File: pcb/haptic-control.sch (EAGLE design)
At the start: 131 parts, among them M1 SPH0641LM4H-1, P1 2P-PAD_1X3.5, P2 2P-PAD_1X3.5, P3 2P-PAD_1X3.5, P4 2P-PAD_1X3.5, U1 MIC23159, U10 DRV2605L, U11 DRV2605L, U12 MTCH6301, U2 BQ51050B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

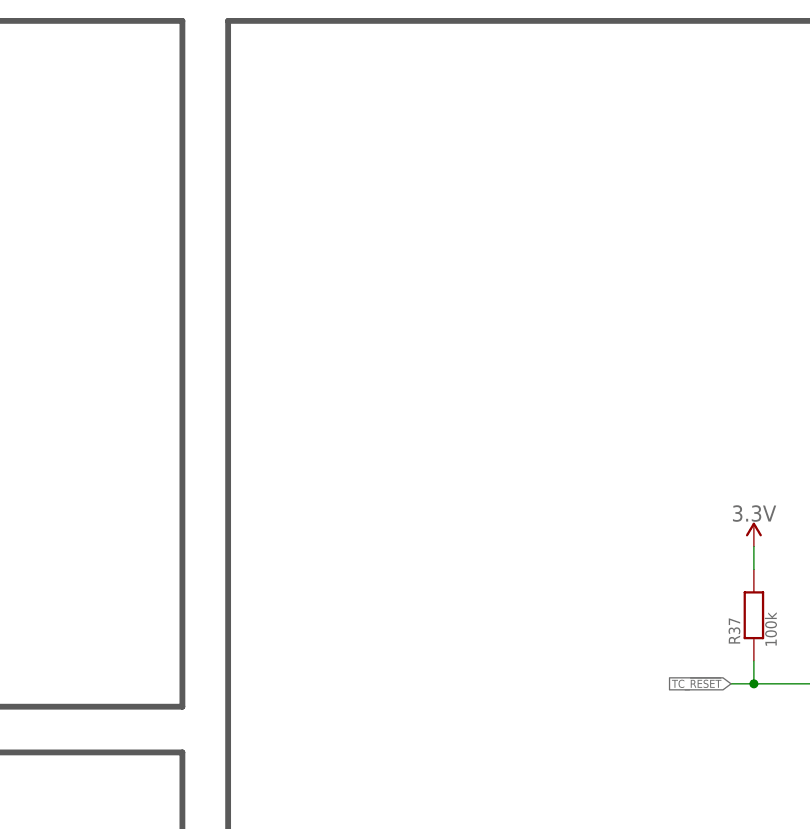
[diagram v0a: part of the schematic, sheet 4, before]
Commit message: Add pcap touch panel
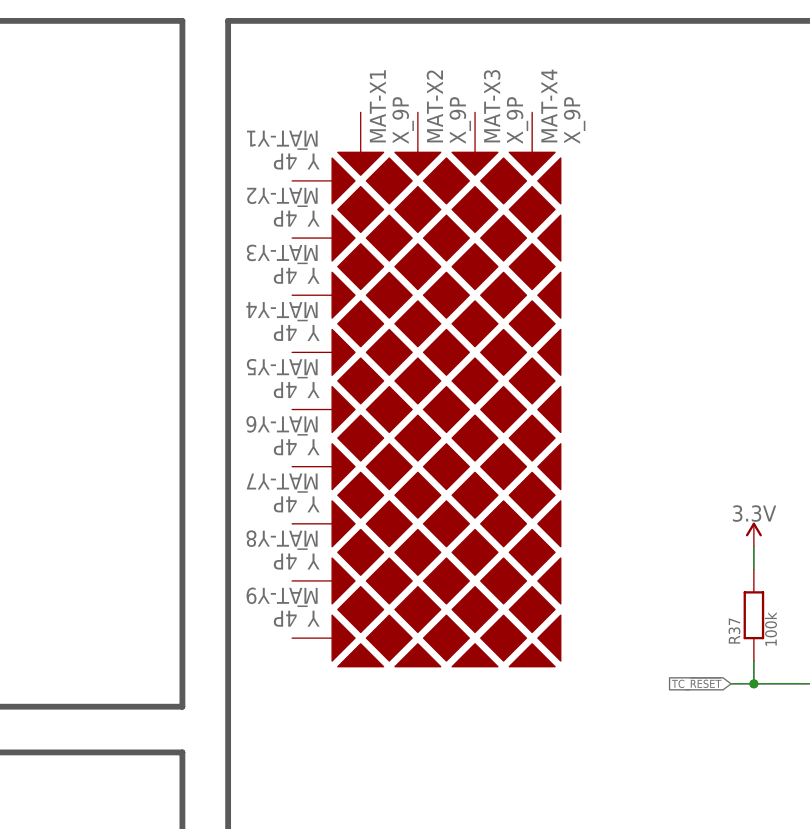
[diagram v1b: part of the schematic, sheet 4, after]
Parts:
- added MAT-X1, MAT-X2, MAT-X3, MAT-X4: X_9P, Touch Panel:X_9P
- added MAT-Y1, MAT-Y2, MAT-Y3, MAT-Y4, MAT-Y5, MAT-Y6, MAT-Y7, MAT-Y8, MAT-Y9: Y_4P, Touch Panel:Y_4P
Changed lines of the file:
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@@
 <part name="C11" library="Passive Components &gt; Capacitors &gt; Multilayer Ceramic Capacitors MLCC" deviceset="MLCC" device="_0402" value="470n"/>
 <part name="JP3" library="Utility &gt; Board" deviceset="JUMPER-SMT_2_NC_TRACE" device="_SILK"/>
+<part name="MAT-X1" library="Touch Panel" deviceset="X_9P" device=""/>
+<part name="MAT-X2" library="Touch Panel" deviceset="X_9P" device=""/>
+<part name="MAT-X3" library="Touch Panel" deviceset="X_9P" device=""/>
+<part name="MAT-X4" library="Touch Panel" deviceset="X_9P" device=""/>
+<part name="MAT-Y1" library="Touch Panel" deviceset="Y_4P" device=""/>
+<part name="MAT-Y2" library="Touch Panel" deviceset="Y_4P" device=""/>
+<part name="MAT-Y3" library="Touch Panel" deviceset="Y_4P" device=""/>
+<part name="MAT-Y4" library="Touch Panel" deviceset="Y_4P" device=""/>
+<part name="MAT-Y5" library="Touch Panel" deviceset="Y_4P" device=""/>
+<part name="MAT-Y6" library="Touch Panel" deviceset="Y_4P" device=""/>
+<part name="MAT-Y7" library="Touch Panel" deviceset="Y_4P" device=""/>
+<part name="MAT-Y8" library="Touch Panel" deviceset="Y_4P" device=""/>
+<part name="MAT-Y9" library="Touch Panel" deviceset="Y_4P" device=""/>
 </parts>
 <sheets>
@@
 <attribute name="VALUE" x="180.34" y="124.206" size="1.778" layer="96" align="top-center"/>
 </instance>
+<instance part="MAT-X1" gate="G$1" x="228.092" y="203.2" smashed="yes">
+<attribute name="VALUE" x="231.648" y="232.664" size="1.778" layer="96" ratio="10" rot="SR90" align="top-left"/>
+<attribute name="NAME" x="229.108" y="232.664" size="1.778" layer="95" ratio="10" rot="SR90" align="top-left"/>
+</instance>
+<instance part="MAT-X2" gate="G$1" x="234.442" y="203.2" smashed="yes">
+<attribute name="VALUE" x="237.998" y="232.664" size="1.778" layer="96" ratio="10" rot="SR90" align="top-left"/>
+<attribute name="NAME" x="235.458" y="232.664" size="1.778" layer="95" ratio="10" rot="SR90" align="top-left"/>
+</instance>
+<instance part="MAT-X3" gate="G$1" x="240.792" y="203.2" smashed="yes">
+<attribute name="VALUE" x="244.348" y="232.664" size="1.778" layer="96" ratio="10" rot="SR90" align="top-left"/>
+<attribute name="NAME" x="241.808" y="232.664" size="1.778" layer="95" ratio="10" rot="SR90" align="top-left"/>
+</instance>
+<instance part="MAT-X4" gate="G$1" x="247.142" y="203.2" smashed="yes">
+<attribute name="VALUE" x="250.698" y="232.664" size="1.778" layer="96" ratio="10" rot="SR90" align="top-left"/>
+<attribute name="NAME" x="248.158" y="232.664" size="1.778" layer="95" ratio="10" rot="SR90" align="top-left"/>
+</instance>
+<instance part="MAT-Y1" gate="G$1" x="237.617" y="228.6" smashed="yes">
+<attribute name="VALUE" x="223.52" y="229.87" size="1.778" layer="96" ratio="10" rot="SR180" align="top-left"/>
+<attribute name="NAME" x="223.52" y="232.41" size="1.778" layer="95" ratio="10" rot="SR180" align="top-left"/>
+</instance>
+<instance part="MAT-Y2" gate="G$1" x="237.617" y="222.25" smashed="yes">
+<attribute name="VALUE" x="223.52" y="223.52" size="1.778" layer="96" ratio="10" rot="SR180" align="top-left"/>
+<attribute name="NAME" x="223.52" y="226.06" size="1.778" layer="95" ratio="10" rot="SR180" align="top-left"/>
+</instance>
+<instance part="MAT-Y3" gate="G$1" x="237.617" y="215.9" smashed="yes">
+<attribute name="VALUE" x="223.52" y="217.17" size="1.778" layer="96" ratio="10" rot="SR180" align="top-left"/>
+<attribute name="NAME" x="223.52" y="219.71" size="1.778" layer="95" ratio="10" rot="SR180" align="top-left"/>
+</instance>
+<instance part="MAT-Y4" gate="G$1" x="237.617" y="209.55" smashed="yes">
+<attribute name="VALUE" x="223.52" y="210.82" size="1.778" layer="96" ratio="10" rot="SR180" align="top-left"/>
+<attribute name="NAME" x="223.52" y="213.36" size="1.778" layer="95" ratio="10" rot="SR180" align="top-left"/>
+</instance>
+<instance part="MAT-Y5" gate="G$1" x="237.617" y="203.2" smashed="yes">
+<attribute name="VALUE" x="223.52" y="204.47" size="1.778" layer="96" ratio="10" rot="SR180" align="top-left"/>
+<attribute name="NAME" x="223.52" y="207.01" size="1.778" layer="95" ratio="10" rot="SR180" align="top-left"/>
+</instance>
+<instance part="MAT-Y6" gate="G$1" x="237.617" y="196.85" smashed="yes">
+<attribute name="VALUE" x="223.52" y="198.12" size="1.778" layer="96" ratio="10" rot="SR180" align="top-left"/>
+<attribute name="NAME" x="223.52" y="200.66" size="1.778" layer="95" ratio="10" rot="SR180" align="top-left"/>
+</instance>
+<instance part="MAT-Y7" gate="G$1" x="237.617" y="190.5" smashed="yes">
+<attribute name="VALUE" x="223.52" y="191.77" size="1.778" layer="96" ratio="10" rot="SR180" align="top-left"/>
+<attribute name="NAME" x="223.52" y="194.31" size="1.778" layer="95" ratio="10" rot="SR180" align="top-left"/>
+</instance>
+<instance part="MAT-Y8" gate="G$1" x="237.617" y="184.15" smashed="yes">
+<attribute name="VALUE" x="223.52" y="185.42" size="1.778" layer="96" ratio="10" rot="SR180" align="top-left"/>
+<attribute name="NAME" x="223.52" y="187.96" size="1.778" layer="95" ratio="10" rot="SR180" align="top-left"/>
+</instance>
+<instance part="MAT-Y9" gate="G$1" x="237.617" y="177.8" smashed="yes">
+<attribute name="VALUE" x="223.52" y="179.07" size="1.778" layer="96" ratio="10" rot="SR180" align="top-left"/>
+<attribute name="NAME" x="223.52" y="181.61" size="1.778" layer="95" ratio="10" rot="SR180" align="top-left"/>
+</instance>
 </instances>

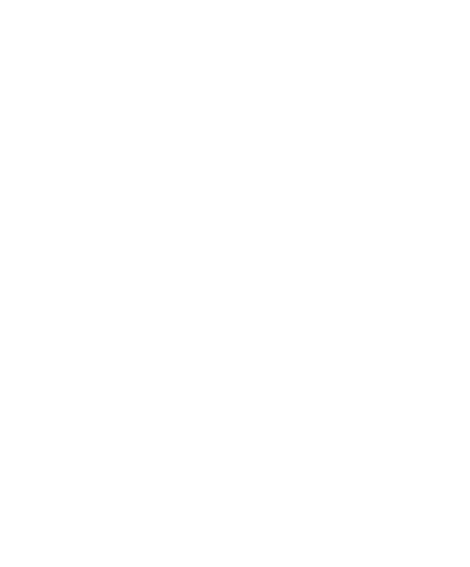
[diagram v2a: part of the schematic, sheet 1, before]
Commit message: Added IPL logo
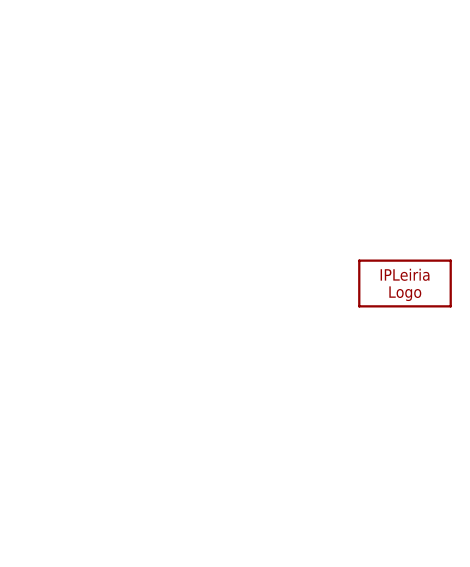
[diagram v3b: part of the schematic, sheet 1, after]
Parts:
- added LOGO1: IPL-10MM, Silkscreen:IPL-10MM
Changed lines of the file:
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@@
 <part name="MAT-Y8" library="Touch Panel" deviceset="Y_4P" device=""/>
 <part name="MAT-Y9" library="Touch Panel" deviceset="Y_4P" device=""/>
+<part name="LOGO1" library="Silkscreen" deviceset="IPL" device="-10MM"/>
 </parts>
 <sheets>
@@
 <attribute name="NAME" x="53.34" y="198.12" size="1.778" layer="95" font="vector"/>
 </instance>
+<instance part="LOGO1" gate="G$1" x="365.76" y="35.56" smashed="yes"/>
 </instances>
 <busses>

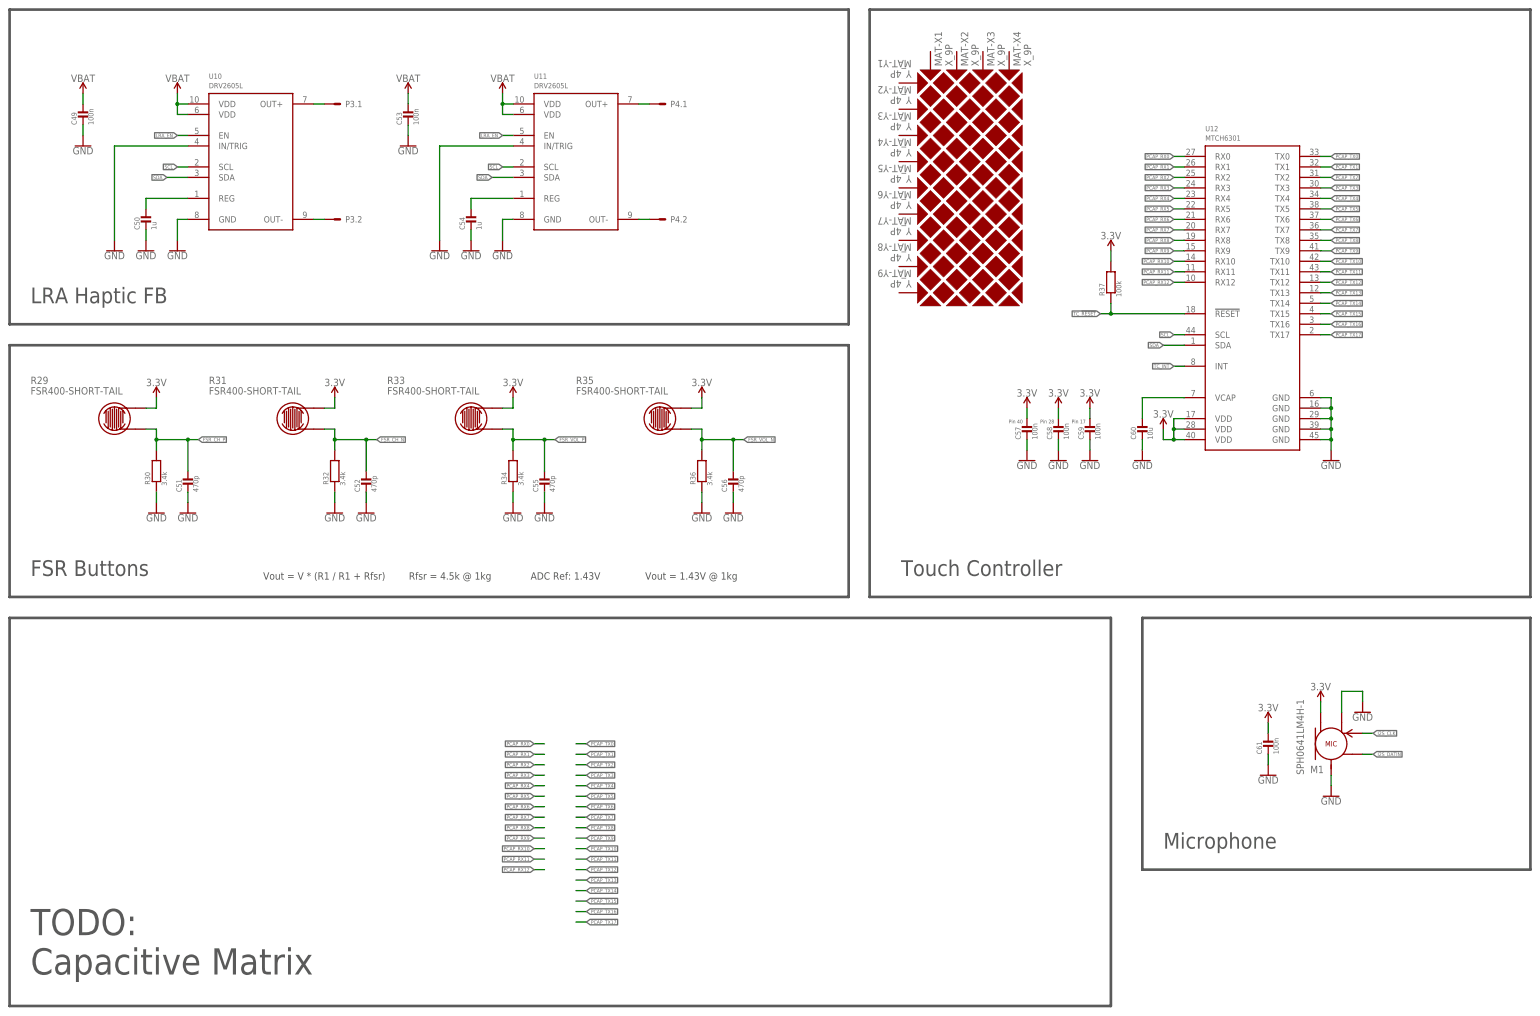
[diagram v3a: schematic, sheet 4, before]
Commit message: touch matrix connections
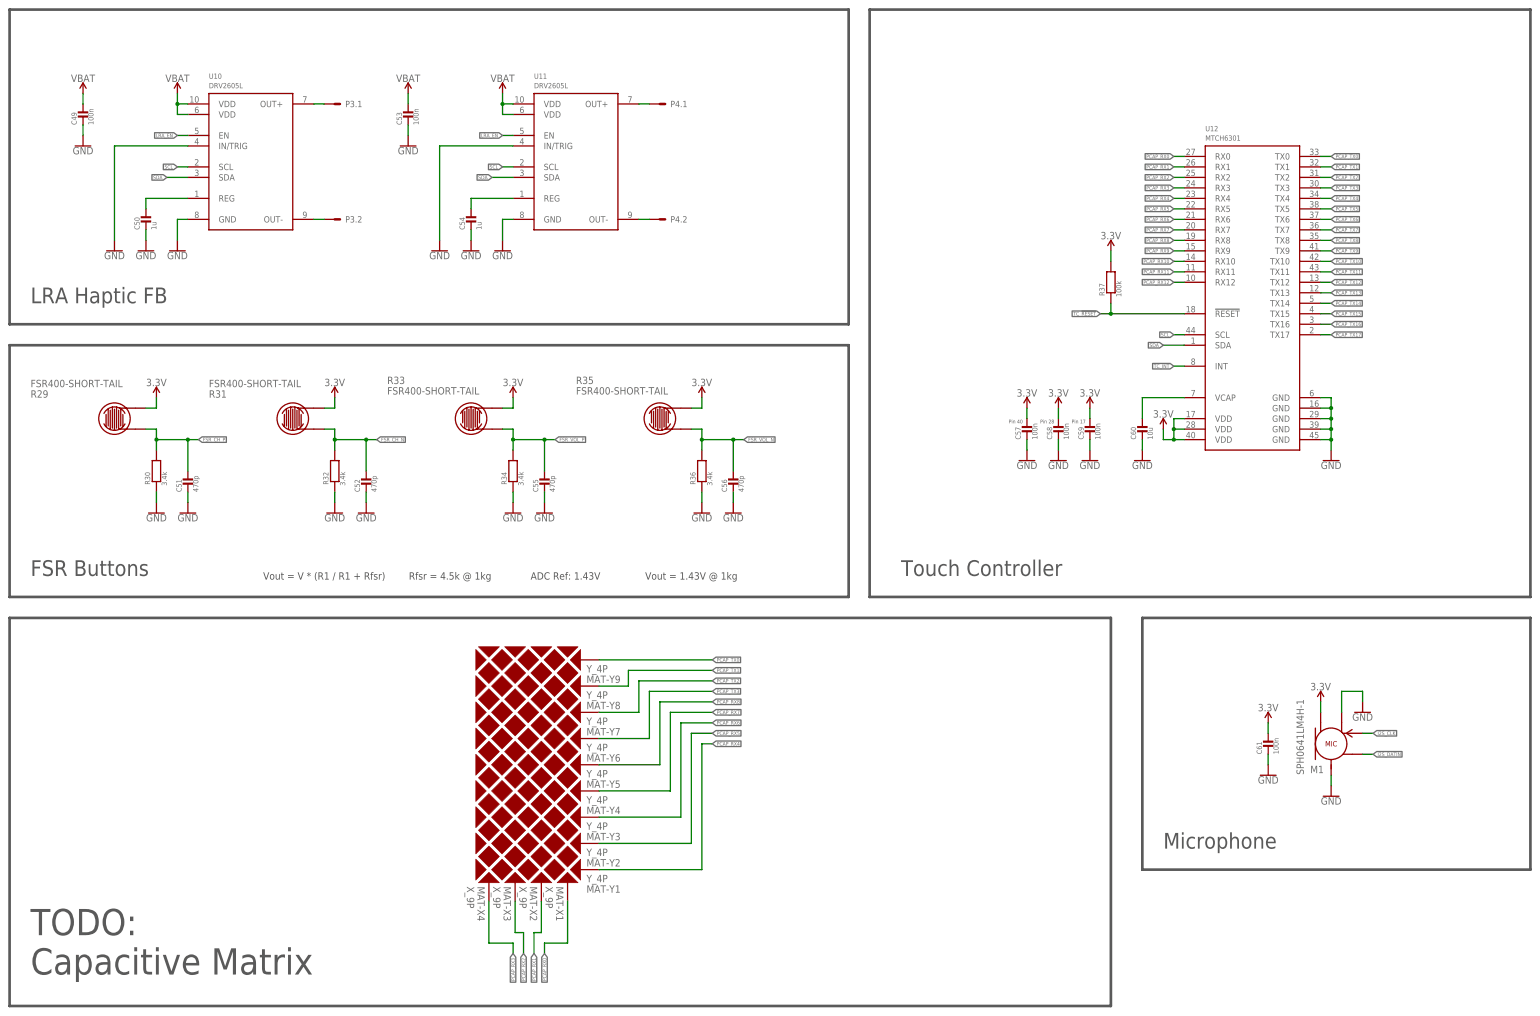
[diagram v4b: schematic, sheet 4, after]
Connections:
- net 3.3V: now also R29.2, R31.2; no longer R29.1, R31.1
- net FSR_CH_N: now also R31.1; no longer R31.2
- net FSR_CH_P: now also R29.1; no longer R29.2
- net PCAP_RX0: now also MAT-X1.1
- net PCAP_RX1: now also MAT-X2.1
- net PCAP_RX2: now also MAT-X3.1
- net PCAP_RX3: now also MAT-X4.1
- net PCAP_RX4: now also MAT-Y1.1
- net PCAP_RX5: now also MAT-Y2.1
- net PCAP_RX6: now also MAT-Y3.1
- net PCAP_RX7: now also MAT-Y4.1
- net PCAP_RX8: now also MAT-Y5.1
- net PCAP_TX0: now also MAT-Y9.1
- net PCAP_TX1: now also MAT-Y8.1
- net PCAP_TX2: now also MAT-Y7.1
- net PCAP_TX3: now also MAT-Y6.1
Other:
- moved on the sheet: MAT-X1, MAT-X2, MAT-X3, MAT-X4, MAT-Y1, MAT-Y2, MAT-Y3, MAT-Y4, MAT-Y5, MAT-Y6, MAT-Y7, MAT-Y8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

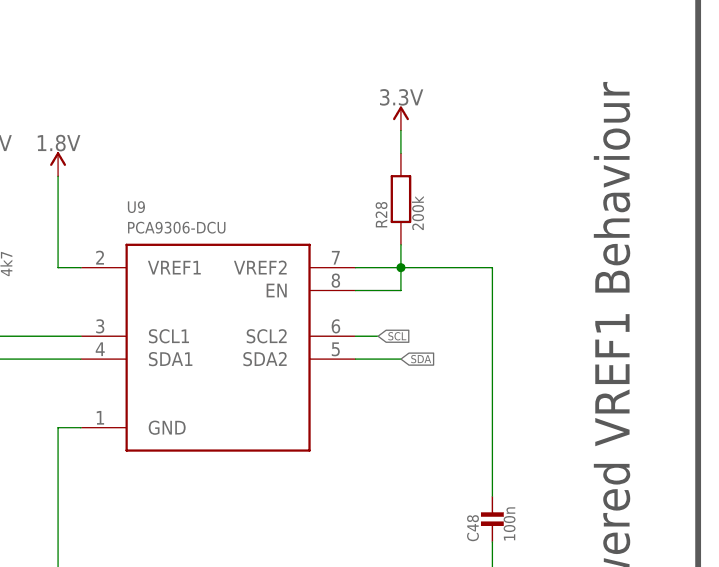
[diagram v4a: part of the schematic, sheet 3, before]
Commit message: i2c level shifter sch fix
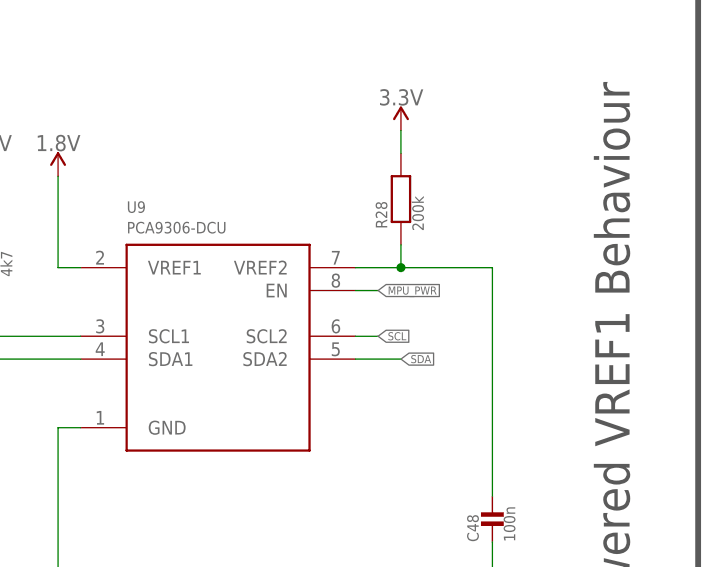
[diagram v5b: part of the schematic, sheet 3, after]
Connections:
- net MPU_PWR: now also U9.EN
- net N$11: no longer U9.EN
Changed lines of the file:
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@@
 <net name="N$11" class="0">
 <segment>
-<pinref part="U9" gate="G$1" pin="EN"/>
-<wire x1="264.16" y1="147.32" x2="269.24" y2="147.32" width="0.1524" layer="91"/>
-<wire x1="269.24" y1="147.32" x2="269.24" y2="149.86" width="0.1524" layer="91"/>
 <pinref part="U9" gate="G$1" pin="VREF2"/>
 <wire x1="264.16" y1="149.86" x2="269.24" y2="149.86" width="0.1524" layer="91"/>
@@
 </segment>
 </net>
+<net name="MPU_PWR" class="0">
+<segment>
+<wire x1="264.16" y1="147.32" x2="266.7" y2="147.32" width="0.1524" layer="91"/>
+<label x="266.7" y="147.32" size="0.889" layer="95" xref="yes"/>
+<pinref part="U9" gate="G$1" pin="EN"/>
+</segment>
+</net>
